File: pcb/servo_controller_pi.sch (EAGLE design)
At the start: 71 parts, among them IC1 PIC18F452, IC3 MAX4173FESA+, IC4 LM2936MP-3.3, IC5 4512D, IC6 LM386M-1, Q1 10Mhz, Q4 BC848ALT1SMD

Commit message: BleuettePi
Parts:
- added T3.3V, T5V, T6V: TPB1,27, testpad:TPB1,27
- added TP1: TPSQPAD1-13, testpad:TPSQPAD1-13
- renumbered SV5 to OPTION
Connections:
- net +3V3: now also T3.3V.TP
- net +5V: now also T5V.TP
- net VEE: now also T6V.TP
- net VSS: now also TP1.TP
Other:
- note added: "Test"
- moved on the sheet: C5, D2, IC3, RSENSE

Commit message: BleuettePi
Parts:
- removed T3.3V, T5V, T6V: TPB1,27, testpad:TPB1,27
- removed U$4: GY-27, gy-27:GY-27
- added AN6, T_3.3V, T_5V, T_6V, T_LVOLTAGE, T_RX_PI, T_TX_PI: TPB1,27, testpad:TPB1,27
- added IC7: GY-27, gy-27:GY-27
- added T_CURRENT: TPSQPAD1-13, testpad:TPSQPAD1-13
- HP+, HP-, P5V, PGND, PLIPO: device wirepad:2,54/0,8 -> wirepad:2,15/1,0
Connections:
- new net N$20: IC1.RE2/!CS/AN7
- new net N$26: AN6.TP, IC1.RE1/!WR/AN6
- net +3V3: now also IC7.VCC, T_3.3V.TP; no longer T3.3V.TP, U$4.VCC
- net +5V: now also T_5V.TP; no longer T5V.TP
- net LIPO_VOLTAGE: now also T_LVOLTAGE.TP
- net RX_PI: now also T_RX_PI.TP
- net SCL: now also IC7.SCL; no longer U$4.SCL
- net SDA: now also IC7.SDA; no longer U$4.SDA
- net SERVO_CURRENT: now also T_CURRENT.TP
- net TX_PI: now also T_TX_PI.TP
- net VEE: now also T_6V.TP; no longer T6V.TP
- net VSS: now also IC7.GND; no longer U$4.GND
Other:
- note removed: "Test"
- moved on the sheet: C12, C5, D2, D3, IC3, R1, R2, RSENSE, TP1

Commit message: RaspberryPi
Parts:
- added DRDY: (no value), jumper:SJ
- U$3: value RASPBERRY-PI -> RASPBERRY-PILIGHT-HOLE; device RaspberryPi:RASPBERRY-PI -> RaspberryPi:RASPBERRY-PILIGHT-HOLE
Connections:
- new net N$36: DRDY.2, IC7.DRY
- net OPTION4: now also DRDY.1
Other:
- moved on the sheet: C12, IC7

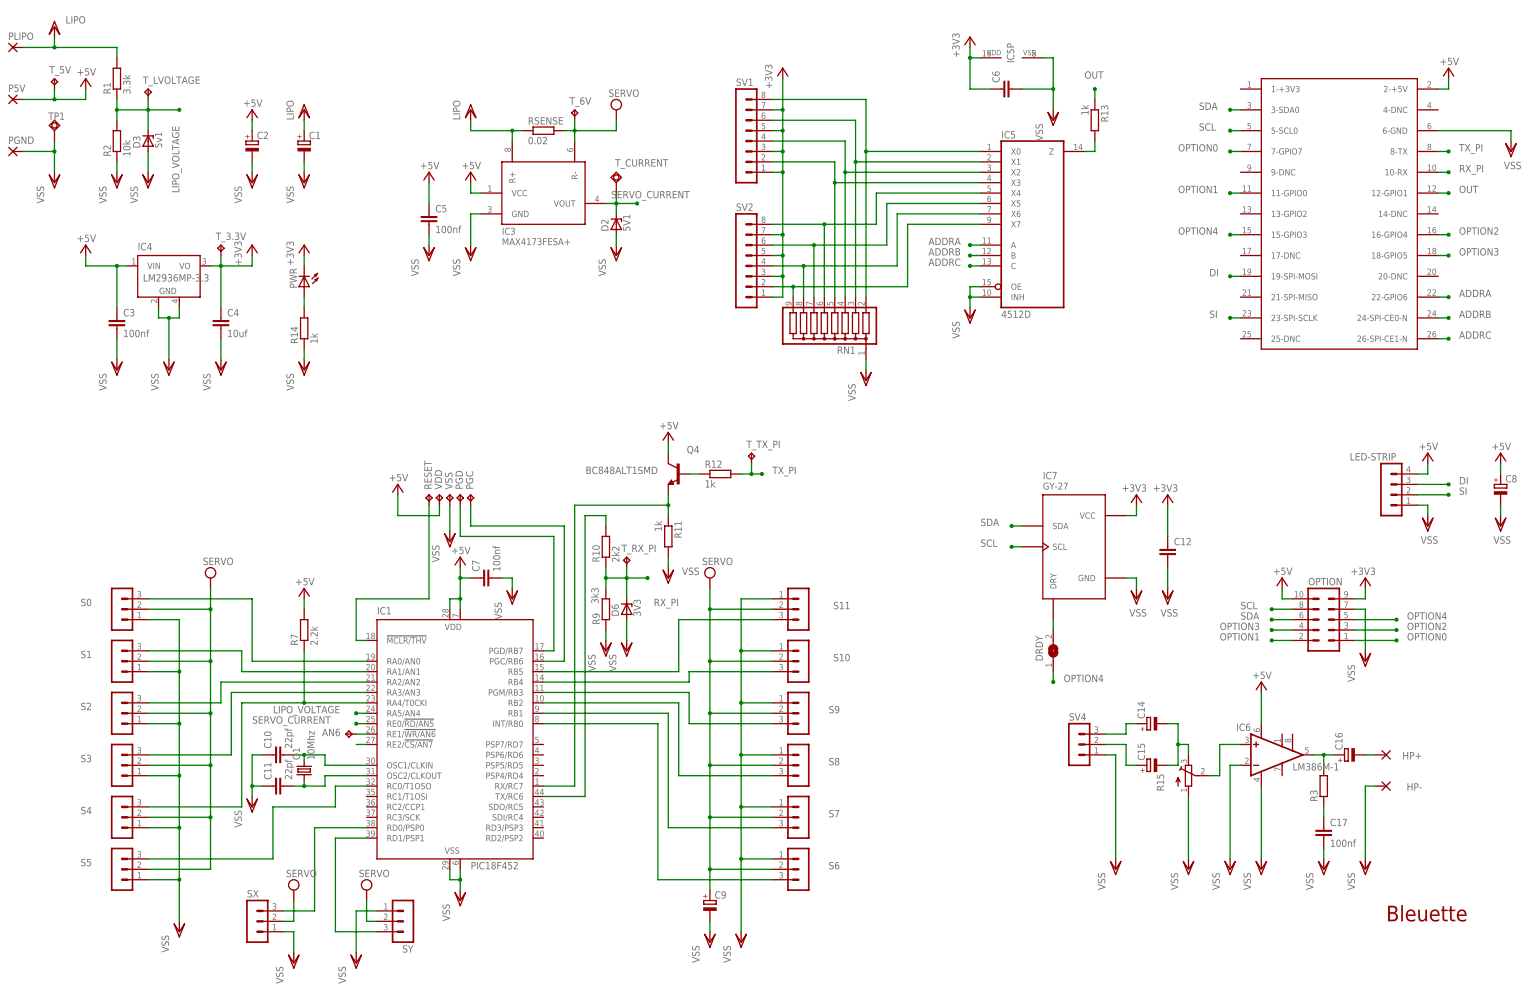
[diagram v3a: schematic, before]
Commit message: Raspberry Pi PCB version
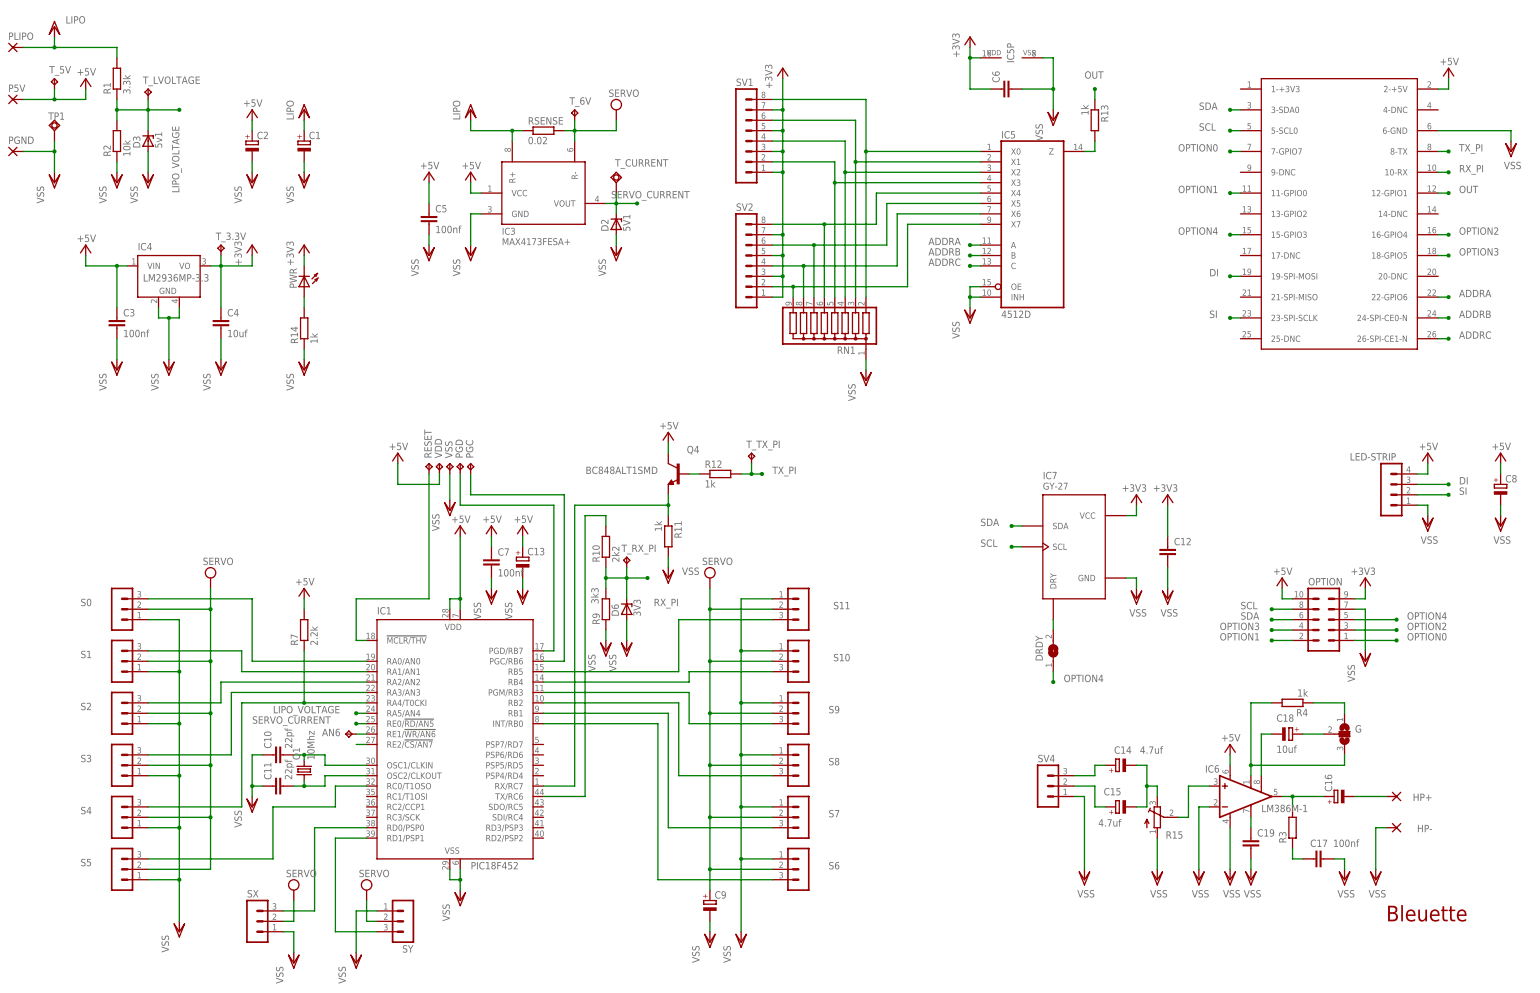
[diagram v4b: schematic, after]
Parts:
- added C13: (no value), rcl:CPOL-EUA
- added C18: 10uf, rcl:CPOL-EUA
- added C19: (no value), rcl:C-EUC0805
- added G: (no value), jumper:SJ2W
- added R4: 1k, rcl:R-EU_M0805
- C14, C15: value (none) -> 4.7uf
- SV1, SV2: device con-lstb:MA08-1W -> con-lstb:MA08-1
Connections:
- new net N$38: G.3, IC6.GAIN@1, R4.2
- new net N$44: G.1, R4.1
- new net N$45: C18.+, G.2
- new net N$46: C18.-, IC6.GAIN@2
- new net N$47: C19.1, IC6.BYPASS
- net +5V: now also C13.+
- net VSS: now also C13.-, C19.2
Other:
- moved on the sheet: C14, C15, C16, C17, C7, HP+, HP-, IC6, PGC, PGD, R15, R3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

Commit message: Raspberry Pi
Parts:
- added AN7, RC1, RC2, RC3, RC4, RC5, RD2, RD3, RD4, RD5, RD6, RD7: TPSQTP06SQ, testpad:TPSQTP06SQ
- added P6V: (no value), wirepad:2,15/1,0
- AN6: value TPB1,27 -> TPSQTP06SQ; device testpad:TPB1,27 -> testpad:TPSQTP06SQ
- renumbered PLIPO to PBATT
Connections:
- new net +7V: C1.+, IC3.R+, P6V.P, RSENSE.1
- new net N$48: IC1.PSP7/RD7, RD7.TP
- new net N$49: IC1.PSP6/RD6, RD6.TP
- new net N$50: IC1.PSP5/RD5, RD5.TP
- new net N$51: IC1.PSP4/RD4, RD4.TP
- new net N$52: IC1.RC2/CCP1, RC2.TP
- new net N$53: IC1.RC1/T1OSI, RC1.TP
- new net N$54: IC1.RC3/SCK, RC3.TP
- new net N$55: IC1.SDI/RC4, RC4.TP
- new net N$56: IC1.SDO/RC5, RC5.TP
- new net N$57: IC1.RD3/PSP3, RD3.TP
- new net N$58: IC1.RD2/PSP2, RD2.TP
- net N$20: now also AN7.TP
- net VDD: no longer C1.+, IC3.R+, RSENSE.1
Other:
- note added: "Son"
- moved on the sheet: C1, C2, C3, C4, D3, D6, DRDY, IC4, OPTION, P5V, PGND, PWR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

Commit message: BleuettePi
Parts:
- removed G: (no value), jumper:SJ2W
- removed Q4: BC848ALT1SMD, transistor-npn:BC848ALT1SMD
- removed R11: 1k, rcl:R-EU_M0805
- removed R15: (no value), pot:TRIM_EU-3223J
- removed RD2: TPSQTP06SQ, testpad:TPSQTP06SQ
- removed SV1, SV2: (no value), con-lstb:MA08-1
- added 1K: (no value), pot:TRIM_EU-3223J
- added C20: (no value), rcl:CPOL-EUA
- added C21: 220uf, rcl:CPOL-EUD
- added D1: 3V3, diode:ZENER-DIODESOT23
- added JP0, JP1, JP2, JP3, JP4, JP5: (no value), pinhead:PINHD-1X2
- added Q2, Q3: BC848ASMD, transistor-npn:BC848ASMD
- added R5: 470, rcl:R-EU_M0805
- added R6: 3k3, rcl:R-EU_M0805
- added R8: 2k2, rcl:R-EU_M0805
- added T_ECHO: TPB1,27, testpad:TPB1,27
- added ULTRASONIC: (no value), con-lstb:MA04-1
- C16: device rcl:CPOL-EUB -> rcl:C-EUC0805
- C17: value 100nf -> 47nf
- C18: value 10uf -> (none); device rcl:CPOL-EUA -> rcl:C-EUC0805
- C19: value (none) -> 100nf
- R3: value (none) -> 10
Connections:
- removed net N$35: IC5A.X7, RN1.9, SV2.2
- removed net N$38: G.3, IC6.GAIN@1, R4.2
- removed net N$45: C18.+, G.2
- removed net N$46: C18.-, IC6.GAIN@2
- removed net N$58: IC1.RD2/PSP2, RD2.TP
- removed net OPTION4: DRDY.1, OPTION.5, U$3.15-GPIO3
- new net ECHO: D1.C, R6.2, R8.1, T_ECHO.TP, U$3.18-GPIO5
- new net INT0: IC1.RD2/PSP2, IC5A.X6
- new net INT1: IC5A.X7, OPTION.5
- new net RX_PIC: IC1.RX/RC7, Q3.C, R4.1
- new net TRIGGER: U$3.15-GPIO3, ULTRASONIC.3
- net +3V3: now also JP0.1, JP1.1, JP2.1, JP3.1, JP4.1, JP5.1; no longer SV1.1, SV1.3, SV1.5, SV1.7, SV2.1, SV2.3, SV2.5, SV2.7
- net +5V: now also C16.1, C18.1, C20.+, R12.2, R4.2, U$3.4-DNC, ULTRASONIC.4; no longer Q4.C
- net N$15: now also R8.2, ULTRASONIC.2; no longer IC1.RX/RC7, Q4.E, R11.1
- net N$18: now also JP5.2; no longer SV2.6
- net N$21: now also Q2.C, Q3.B; no longer Q4.B
- net N$28: now also JP4.2; no longer SV2.8
- net N$29: now also JP3.2; no longer SV1.2
- net N$30: now also JP2.2; no longer SV1.4
- net N$31: now also JP1.2; no longer SV1.6
- net N$33: now also JP0.2; no longer SV1.8
- net N$34: now also DRDY.1; no longer IC5A.X6, RN1.8, SV2.4
- net N$41: now also 1K.S; no longer R15.S
- net N$42: now also C21.+; no longer C16.+
- net N$44: now also Q2.B, R5.2; no longer G.1, R4.1
- net N$7: now also 1K.E; no longer R15.E
- net N$9: now also C21.-; no longer C16.-
- net OPTION3: now also U$3.13-GPIO2; no longer U$3.18-GPIO5
- net TX_PI: now also R5.1; no longer R12.2
- net VSS: now also 1K.A, C16.2, C18.2, C20.-, D1.A, Q2.E, Q3.E, R6.1, U$3.14-DNC, U$3.20-DNC, U$3.25-DNC, U$3.9-DNC, ULTRASONIC.1; no longer R11.2, R15.A
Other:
- moved on the sheet: C14, C15, C17, C19, HP+, HP-, IC6, OPTION, R12, R3, R4, SV4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

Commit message: BleuettePi
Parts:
- added R11, R15: 10, rcl:R-EU_M0805
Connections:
- removed net N$34: DRDY.1
- net +5V: no longer U$3.4-DNC
- net INT1: now also DRDY.1
- net N$41: now also R11.1, R15.2
- net N$7: now also R11.2
- net VSS: now also R15.1; no longer U$3.14-DNC, U$3.20-DNC, U$3.25-DNC, U$3.9-DNC
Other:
- moved on the sheet: 1K, C14, C15, SV4

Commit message: BleuettePi
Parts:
- removed IC5: 4512D, 45xx:4512D
- removed JP0, JP1, JP2, JP3, JP4, JP5: (no value), pinhead:PINHD-1X2
- removed RN1: (no value), resistor-sil:G08R
- added C22: 100nf, rcl:C-EUC0805
- added C24: 10uf, rcl:CPOL-EUCT3528
- added D4, D5, D7: 5V1, diode:ZENER-DIODESOT23
- added DRDY1: (no value), jumper:SJ
- added I2C: (no value), con-lstb:MA04-1
- added IC2: DS1307, eagleParts:DS1307
- added IC8: MCP23017SO, adafruit:MCP23017SO
- added Q4, Q5: (no value), adafruit:MOSFET-NREFLOW
- added R16, R17, R18, R19, R20, R21, R22: 10k, rcl:R-EU_M0805
- added SJ1, SJ2: (no value), jumper:SJ2W
- added SV2: (no value), con-lstb:MA08-2
- added SV3: (no value), con-lstb:MA05-2
- added U$1: MCP3424-E/ST, eagleParts_MCP3424:MCP3424-E/ST
- R13: value 1k -> 10k
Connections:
- removed net ADDRA: IC5A.A, U$3.22-GPIO6
- removed net ADDRB: IC5A.B, U$3.24-SPI-CE0-N
- removed net ADDRC: IC5A.C, U$3.26-SPI-CE1-N
- removed net N$18: IC5A.X5, JP5.2, RN1.7
- removed net N$28: IC5A.X4, JP4.2, RN1.6
- removed net N$29: IC5A.X3, JP3.2, RN1.5
- removed net N$30: IC5A.X2, JP2.2, RN1.4
- removed net N$31: IC5A.X1, JP1.2, RN1.3
- removed net N$33: IC5A.X0, JP0.2, RN1.2
- removed net N$37: IC5A.Z, R13.2
- new net GPA0: IC8.GPA0, SV2.2
- new net GPA1: IC8.GPA1, SV2.4
- new net GPA2: IC8.GPA2, SV2.6
- new net GPA3: IC8.GPA3, SV2.8
- new net GPA4: IC8.GPA4, SV2.10
- new net GPA5: IC8.GPA5, SV2.12
- new net GPA6: IC8.GPA6, SV2.14
- new net GPA7: IC8.GPA7, SV2.16
- new net GPB0: IC8.GPB0, SV3.2
- new net GPB1: IC8.GPB1, SV3.1
- new net GPB2: IC8.GPB2, SV3.4
- new net GPB3: IC8.GPB3, SV3.3
- new net GPB4: IC8.GPB4, SV3.6
- new net GPB5: IC8.GPB5, SV3.5
- new net GPB6: IC8.GPB6, SV3.8
- new net GPB7: IC8.GPB7, SV3.7
- new net INTA: IC8.INTA, U$3.22-GPIO6
- new net INTB: IC8.INTB, U$3.24-SPI-CE0-N
- new net MCP_LIPO_VOLTAGE: SJ1.3, U$1.CH3+
- new net MCP_SERVO_CURRENT: SJ2.3, U$1.CH4+
- new net PIC_LIPO_VOLTAGE: IC1.RA5/AN4, SJ1.1
- new net PIC_SERVO_CURRENT: IC1.RE0/!RD/AN5, SJ2.1
- new net PI_SCL: Q4.S, R16.1, U$3.5-SCL0
- new net PI_SDA: Q5.S, R13.1, U$3.3-SDA0
- new net __: U$3.26-SPI-CE1-N
- net +3V3: now also I2C.4, Q4.G, Q5.G, R13.2, R16.2; no longer C6.1, IC5P.VDD, JP0.1, JP1.1, JP2.1, JP3.1, JP4.1, JP5.1
- net +5V: now also C22.1, C24.+, C6.2, IC8.!RESET, IC8.VDD, R17.2, R18.2, SV3.10, U$1.VDD
- net INT0: no longer IC5A.X6
- net INT1: no longer IC5A.X7
- net LIPO_VOLTAGE: now also SJ1.2; no longer IC1.RA5/AN4
- net OUT: no longer R13.1
- net SCL: now also I2C.3, IC8.SCL, Q4.D, R17.1, U$1.SCL; no longer U$3.5-SCL0
- net SDA: now also I2C.2, IC8.SDA, Q5.D, R18.1, U$1.SDA; no longer U$3.3-SDA0
- net SERVO_CURRENT: now also SJ2.2; no longer IC1.RE0/!RD/AN5
- net VSS: now also C22.2, C24.-, C6.1, I2C.1, IC8.A0, IC8.A1, IC8.A2, IC8.VSS, SV2.1, SV2.11, SV2.13, SV2.15, SV2.3, SV2.5, SV2.7, SV2.9, SV3.9, U$1.ADR0, U$1.ADR1, U$1.CH1-, U$1.CH2-, U$1.CH3-, U$1.CH4-, U$1.VSS; no longer C6.2, IC5A.INH, IC5A.OE, IC5P.VSS, RN1.1
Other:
- note added: "ADC"
- note added: "I/O"
- note added: "Level adapter"
- note added: "Vérifier la taille de C24 qui doit être de 10uf / tantale"
- note removed: "Interface"
- note removed: "Sensors"
- moved on the sheet: 1K, AN6, AN7, C10, C11, C12, C13, C14, C15, C16, C17, C18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
